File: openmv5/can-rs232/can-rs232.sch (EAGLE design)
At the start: 92 parts, among them IC1 TPS613222ADBVR, IC2 AP64060WU-7, IC3 LM321LVIDCKR, IC4 74LVC1G07GW,125, IC5 SN65C3221EPWR, IC6 MCP2542FD-E_SN, J1 OPENMV5-TOP, J2 1771088, Q1 SSM3J356R,LF, U1 74LVC1G17SE-7

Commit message: Fix part
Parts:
- R5, R9: MPN 0603WAJ0471T5E -> CR0603-FX-4700ELF
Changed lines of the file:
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@@
 </pinmapping>
 </spice>
-<attribute name="MPN" value="0603WAJ0471T5E"/>
+<attribute name="MPN" value="CR0603-FX-4700ELF"/>
 </part>
 <part name="SUPPLY3" library="SparkFun-PowerSymbols" library_urn="urn:adsk.eagle:library:530" deviceset="V_BATT" device=""/>
@@
 </pinmapping>
 </spice>
-<attribute name="MPN" value="0603WAJ0471T5E"/>
+<attribute name="MPN" value="CR0603-FX-4700ELF"/>
 </part>
 <part name="GND7" library="sfe" deviceset="GND" device=""/>

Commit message: Fix wrong resistor value
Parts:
- R10, R12, R13, R14, R15: MPN CRCW04021K00FKEDC -> AC0402FR-1310KL
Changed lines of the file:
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@@
 </part>
 <part name="R10" library="sfe" deviceset="RESISTOR" device="0402-RES" value="10K">
-<attribute name="MPN" value="CRCW04021K00FKEDC"/>
+<attribute name="MPN" value="AC0402FR-1310KL"/>
 </part>
 <part name="GND5" library="sfe" deviceset="GND" device=""/>
@@
 </part>
 <part name="R12" library="sfe" deviceset="RESISTOR" device="0402-RES" value="10K">
-<attribute name="MPN" value="CRCW04021K00FKEDC"/>
+<attribute name="MPN" value="AC0402FR-1310KL"/>
 </part>
 <part name="R13" library="sfe" deviceset="RESISTOR" device="0402-RES" value="10K">
-<attribute name="MPN" value="CRCW04021K00FKEDC"/>
+<attribute name="MPN" value="AC0402FR-1310KL"/>
 </part>
 <part name="L4" library="SRF4532-110Y" deviceset="SRF4532-110Y" device="">
@@
 </part>
 <part name="R14" library="sfe" deviceset="RESISTOR" device="0402-RES" value="10K">
-<attribute name="MPN" value="CRCW04021K00FKEDC"/>
+<attribute name="MPN" value="AC0402FR-1310KL"/>
 </part>
 <part name="R15" library="sfe" deviceset="RESISTOR" device="0402-RES" value="10K">
-<attribute name="MPN" value="CRCW04021K00FKEDC"/>
+<attribute name="MPN" value="AC0402FR-1310KL"/>
 </part>
 <part name="D13" library="CPDQT5V0HE-HF" deviceset="CPDQT5V0HE-HF" device="">

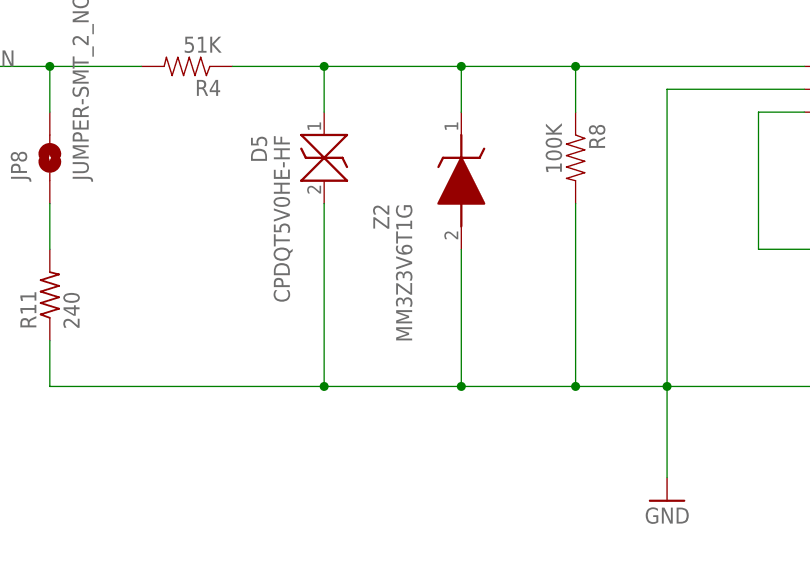
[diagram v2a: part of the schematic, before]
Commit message: Remove zener diode from ADC circuit
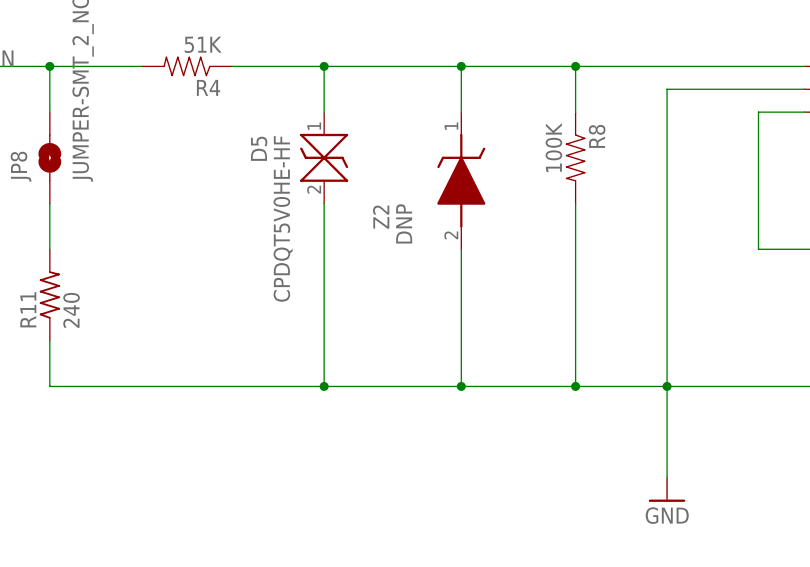
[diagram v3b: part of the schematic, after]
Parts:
- Z2: value MM3Z3V6T1G -> DNP; POPULATE (none) -> 0
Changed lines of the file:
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@@
 </part>
 <part name="GND7" library="sfe" deviceset="GND" device=""/>
-<part name="Z2" library="MM3Z3V6T1G" deviceset="MM3Z3V6T1G" device="">
+<part name="Z2" library="MM3Z3V6T1G" deviceset="MM3Z3V6T1G" device="" value="DNP">
 <attribute name="MPN" value="MM3Z3V6T1G"/>
+<attribute name="POPULATE" value="0"/>
 </part>
 <part name="R11" library="rcl" library_urn="urn:adsk.eagle:library:334" deviceset="R-US_" device="R0603" package3d_urn="urn:adsk.eagle:package:23555/3" value="240">
@@
 <attribute name="VALUE" x="308.61" y="233.68" size="1.778" layer="96" rot="MR270" align="center-left"/>
 <attribute name="MPN" x="314.96" y="243.84" size="1.778" layer="96" rot="MR270" display="off"/>
+<attribute name="POPULATE" x="314.96" y="243.84" size="1.778" layer="96" rot="MR270" display="off"/>
 </instance>
 <instance part="R11" gate="G$1" x="269.24" y="223.52" smashed="yes" rot="R90">
